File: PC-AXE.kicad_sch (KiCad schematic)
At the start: 0 parts

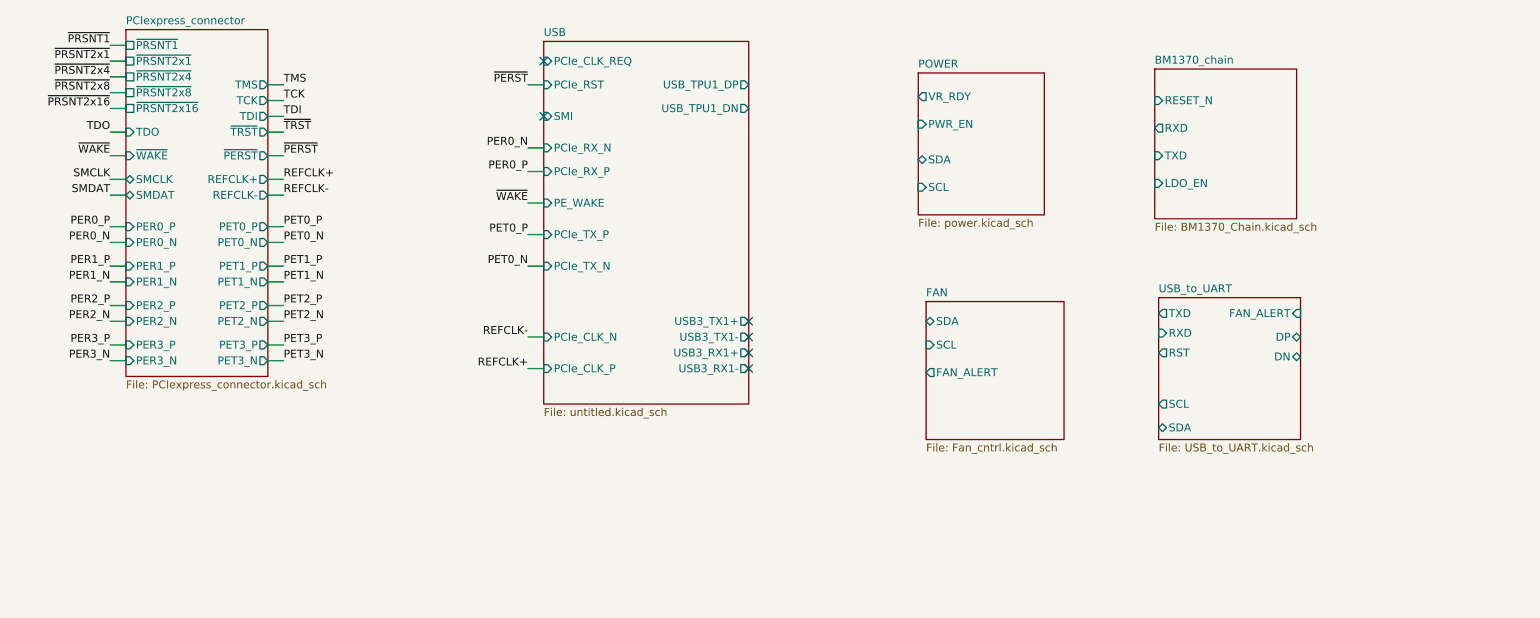
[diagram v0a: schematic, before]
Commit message: board stakup updated and schematic is updated
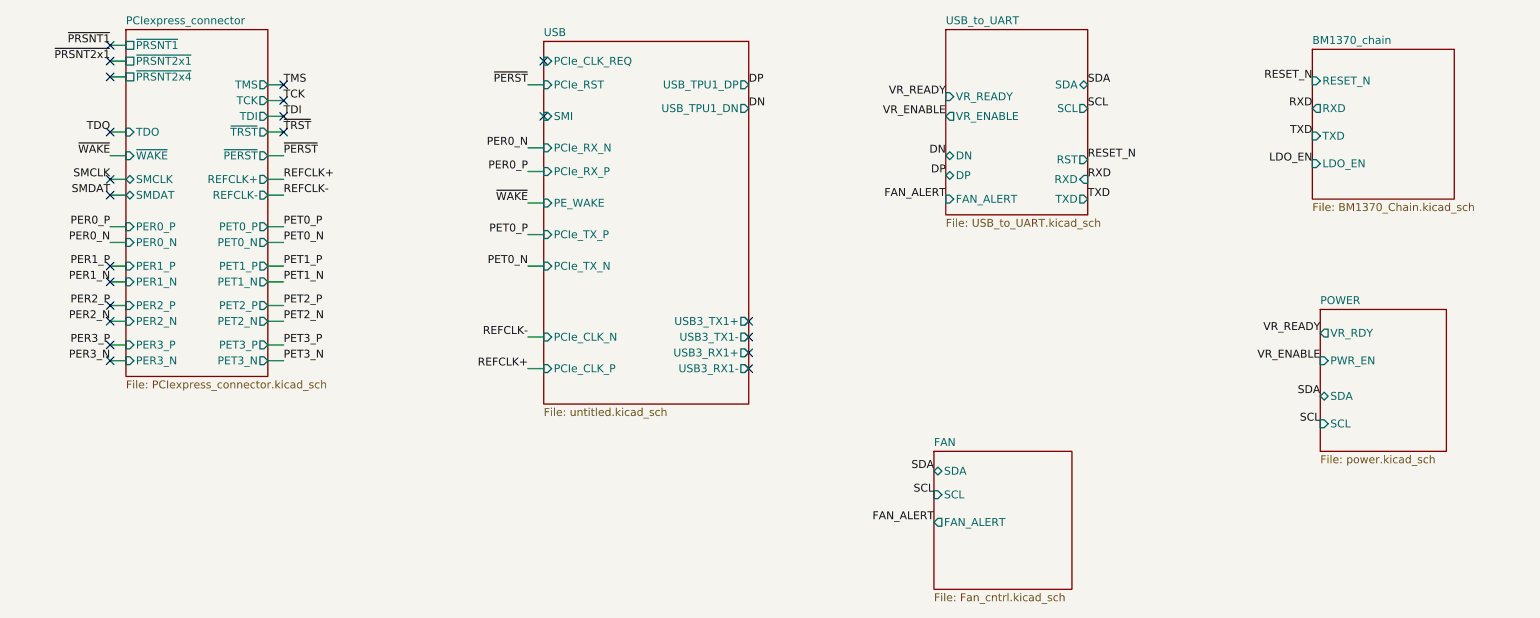
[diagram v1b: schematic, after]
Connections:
- no-connect marks 6 -> 22
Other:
- sheet PCIexpress_connector ports: added none; removed ~{PRSNT2x16}, ~{PRSNT2x8}
- sheet USB_to_UART ports: added VR_ENABLE, VR_READY; removed none

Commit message: updated schematic working on layout
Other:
- company: Author: Luca Anastasio -> Author: Aadhi M
- title: PCIexpress_x4_full -> PC-AXE
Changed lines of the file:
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@@
 	(paper "A4")
 	(title_block
-		(title "PCIexpress_x4_full")
-		(company "Author: Luca Anastasio")
+		(title "PC-AXE")
+		(company "Author: Aadhi M")
 	)
 	(no_connect
